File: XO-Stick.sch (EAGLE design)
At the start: 31 parts, among them J1 POWER, J2 85MOTR, J3 85MOTL, J4 REF, J5 SCL, J6 SDA, J7 AVCC (N/C), J8 AGND (N/C), J9 EXT VCC, SW1 USER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

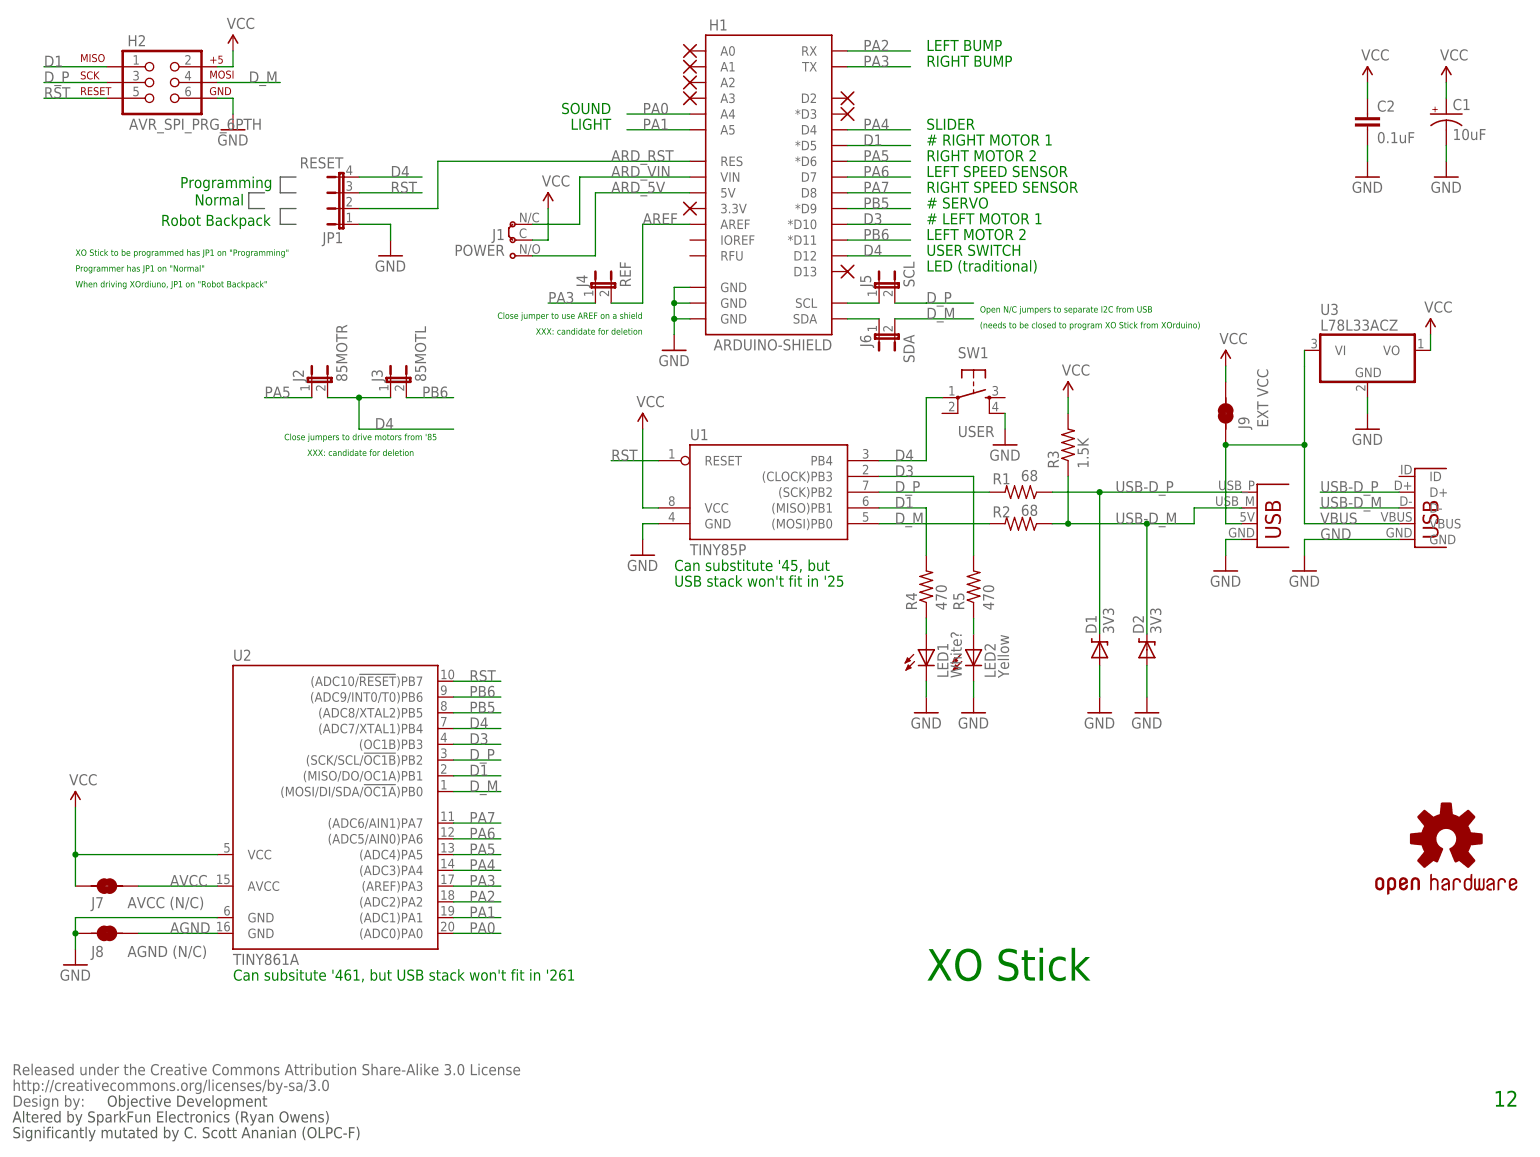
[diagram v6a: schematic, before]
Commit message: XO Stick v13: silkscreen additions; rename nets in schematic for less confusion.
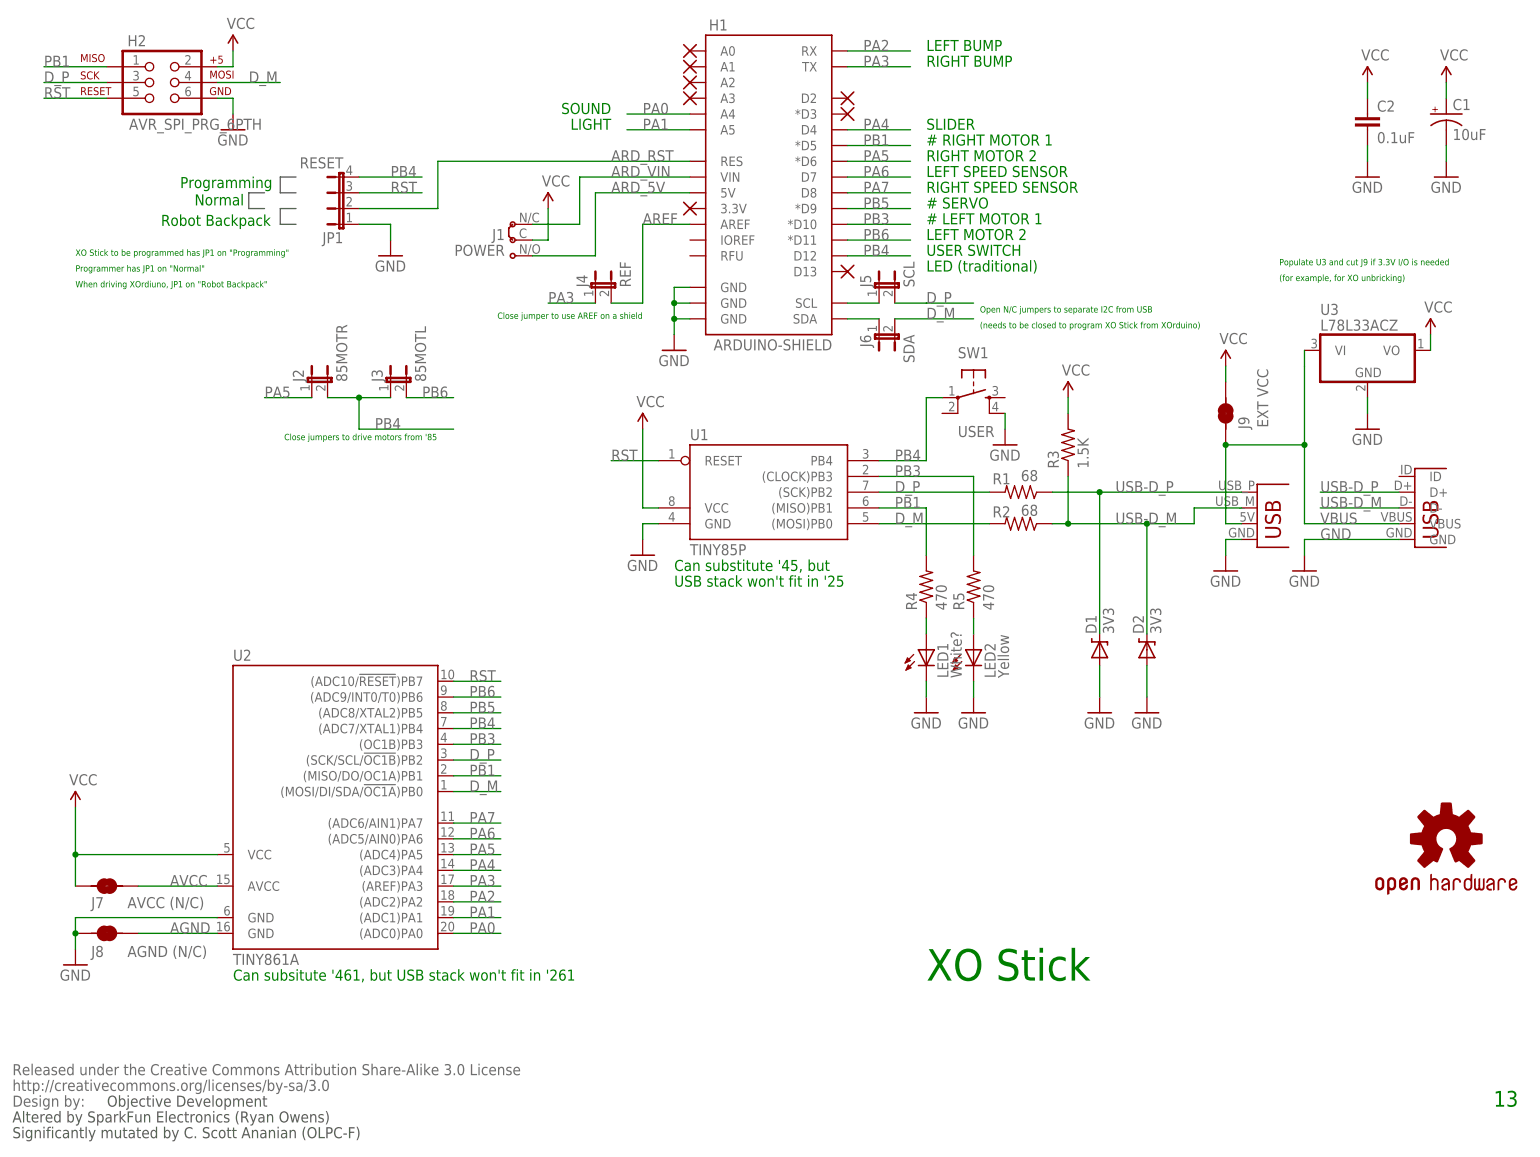
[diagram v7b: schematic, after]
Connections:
- net D1 renamed PB1
- net D3 renamed PB3
- net D4 renamed PB4
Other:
- note added: "(for example, for XO unbricking)"
- note added: "13"
- note added: "Populate U3 and cut J9 if 3.3V I/O is needed"
- note removed: "12"
- note removed: "XXX: candidate for deletion"
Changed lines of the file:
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@@
 <text x="2.54" y="5.08" size="1.778" layer="97">Altered by SparkFun Electronics (Ryan Owens)</text>
 <text x="149.86" y="27.94" size="5.08" layer="91">XO Stick</text>
-<text x="241.3" y="7.62" size="2.54" layer="91">12</text>
+<text x="241.3" y="7.62" size="2.54" layer="91">13</text>
 <text x="149.86" y="162.56" size="1.778" layer="91"># RIGHT MOTOR 1</text>
 <text x="149.86" y="152.4" size="1.778" layer="91"># SERVO</text>
@@
 <text x="12.7" y="139.7" size="1.016" layer="91">When driving XOrdiuno, JP1 on "Robot Backpack"</text>
 <text x="104.14" y="134.62" size="1.016" layer="91" align="bottom-right">Close jumper to use AREF on a shield</text>
-<text x="58.674" y="112.522" size="1.016" layer="91" align="bottom-center">XXX: candidate for deletion</text>
-<text x="104.14" y="132.08" size="1.016" layer="91" align="bottom-right">XXX: candidate for deletion</text>
 <text x="158.496" y="133.096" size="1.016" layer="91">(needs to be closed to program XO Stick from XOrduino)</text>
 <text x="38.1" y="27.94" size="1.778" layer="91">Can subsitute '461, but USB stack won't fit in '261</text>
 <text x="109.22" y="93.98" size="1.778" layer="91">Can substitute '45, but</text>
 <text x="109.22" y="91.44" size="1.778" layer="91">USB stack won't fit in '25</text>
+<text x="206.756" y="143.256" size="1.016" layer="91">Populate U3 and cut J9 if 3.3V I/O is needed</text>
+<text x="206.756" y="140.716" size="1.016" layer="91">(for example, for XO unbricking)</text>
 </plain>
 <instances>
@@
 </segment>
 </net>
-<net name="D1" class="0">
+<net name="PB1" class="0">
 <segment>
 <wire x1="142.24" y1="104.14" x2="149.86" y2="104.14" width="0.1524" layer="91"/>
@@
 </segment>
 </net>
-<net name="D3" class="0">
+<net name="PB3" class="0">
 <segment>
 <wire x1="142.24" y1="109.22" x2="157.48" y2="109.22" width="0.1524" layer="91"/>
@@
 </segment>
 </net>
-<net name="D4" class="0">
+<net name="PB4" class="0">
 <segment>
 <wire x1="73.66" y1="68.58" x2="81.28" y2="68.58" width="0.1524" layer="91"/>
